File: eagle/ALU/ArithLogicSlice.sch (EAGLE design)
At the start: 0 parts

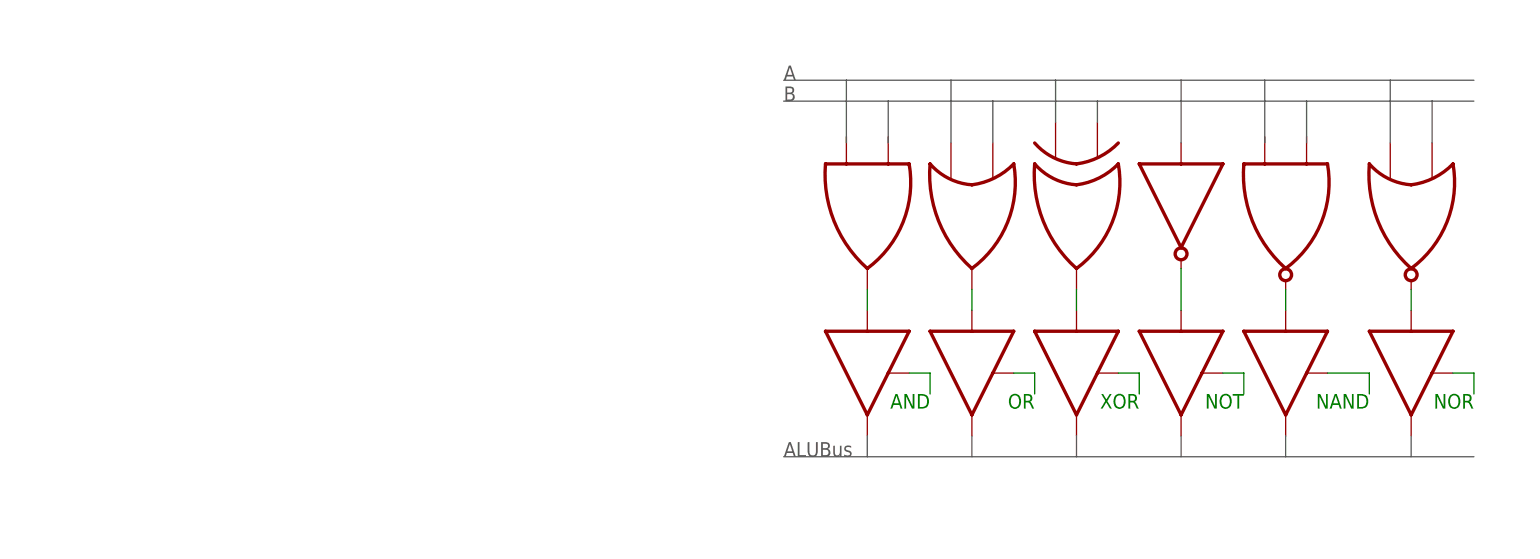
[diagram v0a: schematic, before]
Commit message: FR:ALU design reduction and rewording
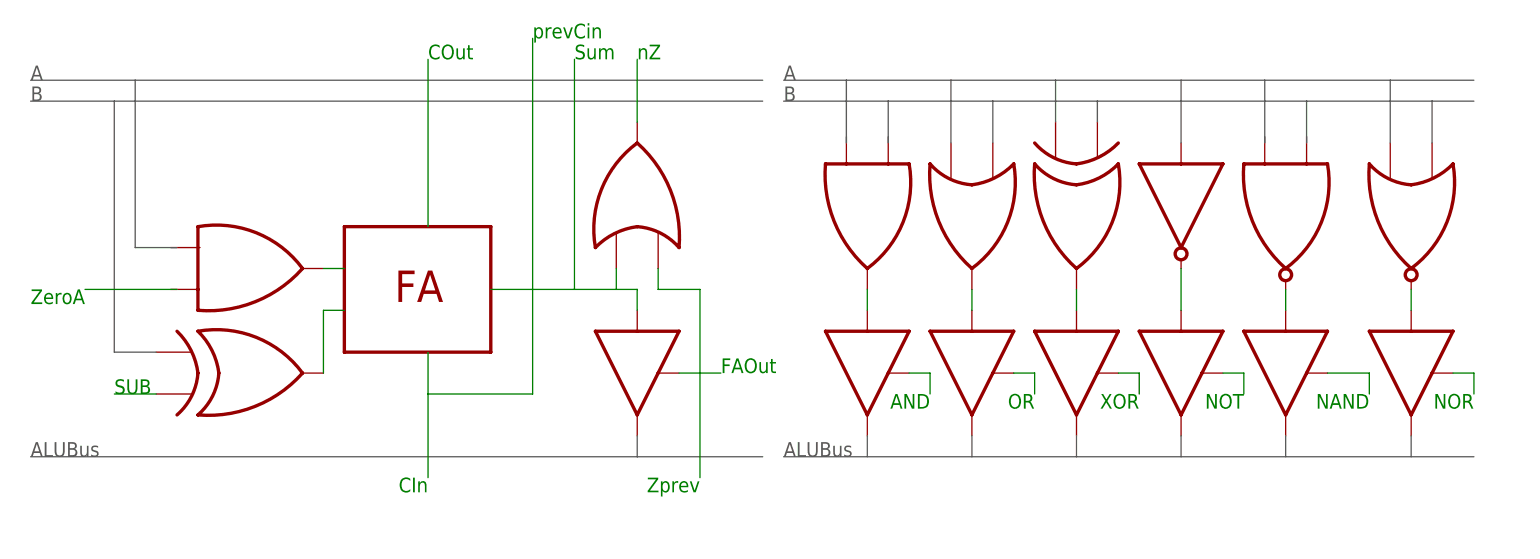
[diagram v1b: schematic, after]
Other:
- note added: "CIn"
- note added: "COut"
- note added: "FA"
- note added: "FAOut"
- note added: "SUB"
- note added: "Sum"
- note added: "ZeroA"
- note added: "Zprev"
- note added: "nZ"
- note added: "prevCin"
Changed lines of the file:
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@@
 <text x="63.5" y="86.36" size="1.778" layer="91" rot="R180">NAND</text>
 <text x="76.2" y="86.36" size="1.778" layer="91" rot="R180">NOR</text>
+<wire x1="-60.96" y1="106.68" x2="-43.18" y2="106.68" width="0.4064" layer="94"/>
+<wire x1="-43.18" y1="106.68" x2="-43.18" y2="91.44" width="0.4064" layer="94"/>
+<wire x1="-43.18" y1="91.44" x2="-60.96" y2="91.44" width="0.4064" layer="94"/>
+<wire x1="-60.96" y1="91.44" x2="-60.96" y2="106.68" width="0.4064" layer="94"/>
+<text x="-54.864" y="97.536" size="3.81" layer="94">FA</text>
+<wire x1="-30.48" y1="104.14" x2="-25.4" y2="116.84" width="0.4064" layer="94" curve="-63.434949"/>
+<wire x1="-20.32" y1="104.14" x2="-25.4" y2="116.84" width="0.4064" layer="94" curve="53.130102"/>
+<wire x1="-25.4" y1="106.68" x2="-20.32" y2="104.14" width="0.4064" layer="94" curve="-45"/>
+<wire x1="-25.4" y1="106.68" x2="-30.48" y2="104.14" width="0.4064" layer="94" curve="38.659808"/>
+<wire x1="-27.94" y1="101.6" x2="-27.94" y2="105.918" width="0.1524" layer="94"/>
+<wire x1="-22.86" y1="101.6" x2="-22.86" y2="105.918" width="0.1524" layer="94"/>
+<wire x1="-25.4" y1="116.84" x2="-25.4" y2="119.38" width="0.1524" layer="94"/>
+<wire x1="-78.74" y1="93.98" x2="-66.04" y2="88.9" width="0.4064" layer="94" curve="-63.434949"/>
+<wire x1="-78.74" y1="83.82" x2="-66.04" y2="88.9" width="0.4064" layer="94" curve="53.130102"/>
+<wire x1="-76.2" y1="88.9" x2="-78.74" y2="83.82" width="0.4064" layer="94" curve="-45"/>
+<wire x1="-76.2" y1="88.9" x2="-78.74" y2="93.98" width="0.4064" layer="94" curve="38.659808"/>
+<wire x1="-66.04" y1="88.9" x2="-63.5" y2="88.9" width="0.1524" layer="94"/>
+<wire x1="-83.82" y1="86.36" x2="-79.502" y2="86.36" width="0.1524" layer="94"/>
+<wire x1="-83.82" y1="91.44" x2="-79.502" y2="91.44" width="0.1524" layer="94"/>
+<wire x1="-78.74" y1="88.9" x2="-81.28" y2="93.98" width="0.4064" layer="94" curve="38.659808"/>
+<wire x1="-78.74" y1="88.9" x2="-81.28" y2="83.82" width="0.4064" layer="94" curve="-45"/>
+<wire x1="-30.48" y1="93.98" x2="-25.4" y2="93.98" width="0.4064" layer="94"/>
+<wire x1="-25.4" y1="93.98" x2="-20.32" y2="93.98" width="0.4064" layer="94"/>
+<wire x1="-20.32" y1="93.98" x2="-22.86" y2="88.9" width="0.4064" layer="94"/>
+<wire x1="-22.86" y1="88.9" x2="-25.4" y2="83.82" width="0.4064" layer="94"/>
+<wire x1="-25.4" y1="83.82" x2="-30.48" y2="93.98" width="0.4064" layer="94"/>
+<wire x1="-25.4" y1="93.98" x2="-25.4" y2="96.52" width="0.1524" layer="94"/>
+<wire x1="-22.86" y1="88.9" x2="-20.32" y2="88.9" width="0.1524" layer="94"/>
+<wire x1="-25.4" y1="83.82" x2="-25.4" y2="81.28" width="0.1524" layer="94"/>
+<text x="-99.06" y="124.46" size="1.778" layer="92">A</text>
+<text x="-99.06" y="121.92" size="1.778" layer="92">B</text>
+<text x="-99.06" y="78.74" size="1.778" layer="92">ALUBus</text>
+<text x="-88.9" y="86.36" size="1.778" layer="91">SUB</text>
+<text x="-92.456" y="99.06" size="1.778" layer="91" rot="R180">ZeroA</text>
+<wire x1="-78.74" y1="106.68" x2="-66.04" y2="101.6" width="0.4064" layer="94" curve="-63.434949"/>
+<wire x1="-78.74" y1="96.52" x2="-66.04" y2="101.6" width="0.4064" layer="94" curve="53.130102"/>
+<wire x1="-82.042" y1="104.14" x2="-78.486" y2="104.14" width="0.1524" layer="94"/>
+<wire x1="-82.042" y1="99.06" x2="-78.74" y2="99.06" width="0.1524" layer="94"/>
+<wire x1="-66.04" y1="101.6" x2="-63.5" y2="101.6" width="0.1524" layer="94"/>
+<wire x1="-78.74" y1="106.68" x2="-78.74" y2="99.06" width="0.4064" layer="94"/>
+<wire x1="-78.74" y1="99.06" x2="-78.74" y2="96.52" width="0.4064" layer="94"/>
+<text x="-50.8" y="127" size="1.778" layer="91">COut</text>
+<text x="-50.8" y="76.2" size="1.778" layer="91" rot="R180">CIn</text>
+<text x="-17.78" y="76.2" size="1.778" layer="91" rot="R180">Zprev</text>
+<text x="-25.4" y="127" size="1.778" layer="91">nZ</text>
+<text x="-33.02" y="127" size="1.778" layer="91">Sum</text>
+<text x="-38.1" y="129.54" size="1.778" layer="91">prevCin</text>
+<text x="-15.24" y="88.9" size="1.778" layer="91">FAOut</text>
 </plain>
 <instances>
@@
 <wire x1="66.04" y1="124.46" x2="66.04" y2="116.84" width="0.1524" layer="92"/>
 </segment>
+<segment>
+<wire x1="-99.06" y1="124.46" x2="-86.36" y2="124.46" width="0.1524" layer="92"/>
+<wire x1="-86.36" y1="124.46" x2="-10.16" y2="124.46" width="0.1524" layer="92"/>
+<wire x1="-86.36" y1="124.46" x2="-86.36" y2="104.14" width="0.1524" layer="92"/>
+<wire x1="-86.36" y1="104.14" x2="-81.28" y2="104.14" width="0.1524" layer="92"/>
+</segment>
 </bus>
 <bus name="B$2">
@@
 <wire x1="71.12" y1="121.92" x2="71.12" y2="116.84" width="0.1524" layer="92"/>
 </segment>
+<segment>
+<wire x1="-99.06" y1="121.92" x2="-88.9" y2="121.92" width="0.1524" layer="92"/>
+<wire x1="-88.9" y1="121.92" x2="-10.16" y2="121.92" width="0.1524" layer="92"/>
+<wire x1="-88.9" y1="121.92" x2="-88.9" y2="91.44" width="0.1524" layer="92"/>
+<wire x1="-88.9" y1="91.44" x2="-83.82" y2="91.44" width="0.1524" layer="92"/>
+</segment>
 </bus>
 <bus name="B$3">
@@
 <segment>
 <wire x1="68.58" y1="78.74" x2="68.58" y2="81.28" width="0.1524" layer="92"/>
+</segment>
+<segment>
+<wire x1="-99.06" y1="78.74" x2="-25.4" y2="78.74" width="0.1524" layer="92"/>
+<wire x1="-25.4" y1="78.74" x2="-10.16" y2="78.74" width="0.1524" layer="92"/>
+<wire x1="-25.4" y1="78.74" x2="-25.4" y2="81.28" width="0.1524" layer="92"/>
 </segment>
 </bus>
@@
 </segment>
 </net>
+<net name="N$13" class="0">
+<segment>
+<wire x1="-63.5" y1="101.6" x2="-60.96" y2="101.6" width="0.1524" layer="91"/>
+</segment>
+</net>
+<net name="N$14" class="0">
+<segment>
+<wire x1="-60.96" y1="96.52" x2="-63.5" y2="96.52" width="0.1524" layer="91"/>
+<wire x1="-63.5" y1="96.52" x2="-63.5" y2="88.9" width="0.1524" layer="91"/>
+</segment>
+</net>
+<net name="N$15" class="0">
+<segment>
+<wire x1="-83.82" y1="86.36" x2="-88.9" y2="86.36" width="0.1524" layer="91"/>
+</segment>
+</net>
+<net name="N$16" class="0">
+<segment>
+<wire x1="-50.8" y1="106.68" x2="-50.8" y2="127" width="0.1524" layer="91"/>
+</segment>
+</net>
+<net name="N$17" class="0">
+<segment>
+<wire x1="-50.8" y1="91.44" x2="-50.8" y2="86.36" width="0.1524" layer="91"/>
+<wire x1="-50.8" y1="86.36" x2="-50.8" y2="76.2" width="0.1524" layer="91"/>
+<wire x1="-50.8" y1="86.36" x2="-38.1" y2="86.36" width="0.1524" layer="91"/>
+<wire x1="-38.1" y1="86.36" x2="-38.1" y2="129.54" width="0.1524" layer="91"/>
+</segment>
+</net>
+<net name="N$18" class="0">
+<segment>
+<wire x1="-43.18" y1="99.06" x2="-33.02" y2="99.06" width="0.1524" layer="91"/>
+<wire x1="-33.02" y1="99.06" x2="-27.94" y2="99.06" width="0.1524" layer="91"/>
+<wire x1="-27.94" y1="99.06" x2="-25.4" y2="99.06" width="0.1524" layer="91"/>
+<wire x1="-25.4" y1="99.06" x2="-25.4" y2="96.52" width="0.1524" layer="91"/>
+<wire x1="-33.02" y1="99.06" x2="-33.02" y2="127" width="0.1524" layer="91"/>
+<wire x1="-27.94" y1="99.06" x2="-27.94" y2="101.6" width="0.1524" layer="91"/>
+</segment>
+</net>
+<net name="N$19" class="0">
+<segment>
+<wire x1="-22.86" y1="99.06" x2="-17.78" y2="99.06" width="0.1524" layer="91"/>
+<wire x1="-17.78" y1="99.06" x2="-17.78" y2="76.2" width="0.1524" layer="91"/>
+<wire x1="-22.86" y1="99.06" x2="-22.86" y2="101.6" width="0.1524" layer="91"/>
+</segment>
+</net>
+<net name="N$20" class="0">
+<segment>
+<wire x1="-25.4" y1="119.38" x2="-25.4" y2="127" width="0.1524" layer="91"/>
+</segment>
+</net>
+<net name="N$21" class="0">
+<segment>
+<wire x1="-81.28" y1="99.06" x2="-92.456" y2="99.06" width="0.1524" layer="91"/>
+</segment>
+</net>
+<net name="N$22" class="0">
+<segment>
+<wire x1="-20.32" y1="88.9" x2="-15.24" y2="88.9" width="0.1524" layer="91"/>
+</segment>
+</net>

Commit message: Eagle schematics now use library
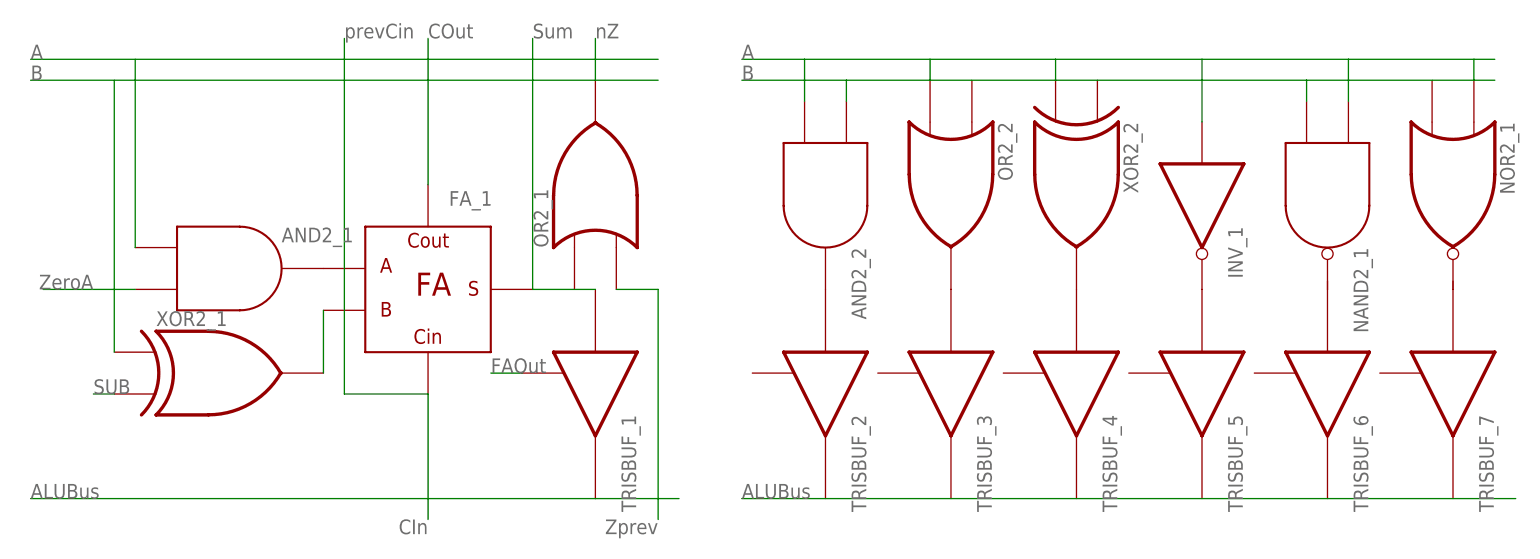
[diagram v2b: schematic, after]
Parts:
- added AND2_1, AND2_2: AND2, c035u:AND2
- added FA_1: FULLADDER, c035u:FULLADDER
- added INV_1: INV, c035u:INV
- added NAND2_1: NAND2, c035u:NAND2
- added NOR2_1: NOR2, c035u:NOR2
- added OR2_1, OR2_2: OR2, c035u:OR2
- added TRISBUF_1, TRISBUF_2, TRISBUF_3, TRISBUF_4, TRISBUF_5, TRISBUF_6, TRISBUF_7: TRISBUF, c035u:TRISBUF
- added XOR2_1, XOR2_2: XOR2, c035u:XOR2
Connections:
- new net N$1: AND2_2.O, TRISBUF_2.I
- new net N$13: AND2_1.O, FA_1.A
- new net N$14: FA_1.B, XOR2_1.O
- new net N$15: XOR2_1.I1
- new net N$16: FA_1.COUT
- new net N$17: TRISBUF_1.P$1
- new net N$18: FA_1.S, OR2_1.I0, TRISBUF_1.I
- new net N$19: OR2_1.I1
- new net N$2: OR2_2.O, TRISBUF_3.I
- new net N$20: OR2_1.O
- new net N$22: TRISBUF_1.O
- new net N$23: XOR2_1.I0
- new net N$24: AND2_1.A
- new net N$25: FA_1.CIN
- new net N$3: TRISBUF_4.I, XOR2_2.O
- new net N$4: INV_1.O, TRISBUF_5.I
- new net N$5: NAND2_1.O, TRISBUF_6.I
- new net N$6: NOR2_1.O, TRISBUF_7.I
- new net N$9: AND2_2.A, AND2_2.I1, INV_1.I, NAND2_1.A, NAND2_1.I1, OR2_2.I1, XOR2_2.I1
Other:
- note removed: "AND"
- note removed: "FA"
- note removed: "NAND"
- note removed: "NOR"
- note removed: "NOT"
- note removed: "OR"
- note removed: "XOR"
